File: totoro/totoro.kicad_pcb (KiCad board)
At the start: 2 copper layers, 82 parts, among them J1 USB_B_Micro, J2 SWR201-NRTN-S02-SA-WH, J3 SWR201-NRTN-S02-SA-WH, Q1 MMBT3904, Q2 MMBT3904, Q3 MMBT3904, Q4 2N7002, Q5 2N7002, Q6 MMBT3904, Q7 BC817, Q8 BC817, SW1 PTS810 SJM 250 SMTR LFS, SW2 KSC441J DCT 70SH LFS, U1 LMR62421XSD, U2 ESP32-WROOM-32, U3 CP2102N-A01-GQFN24, U4 TPS62152, U5 MCP6001R, U6 MCP6001R

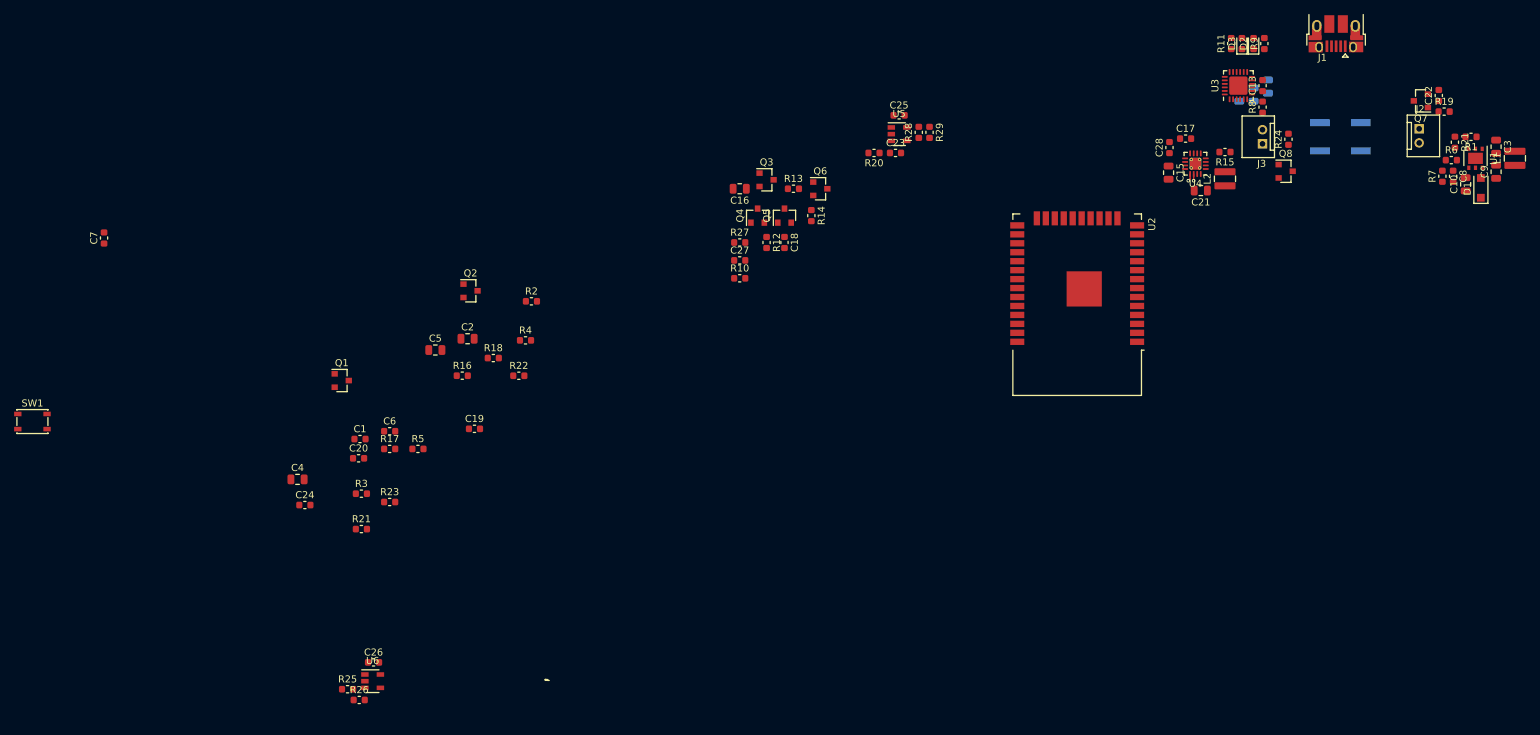
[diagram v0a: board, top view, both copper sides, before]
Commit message: All parts are in the circle
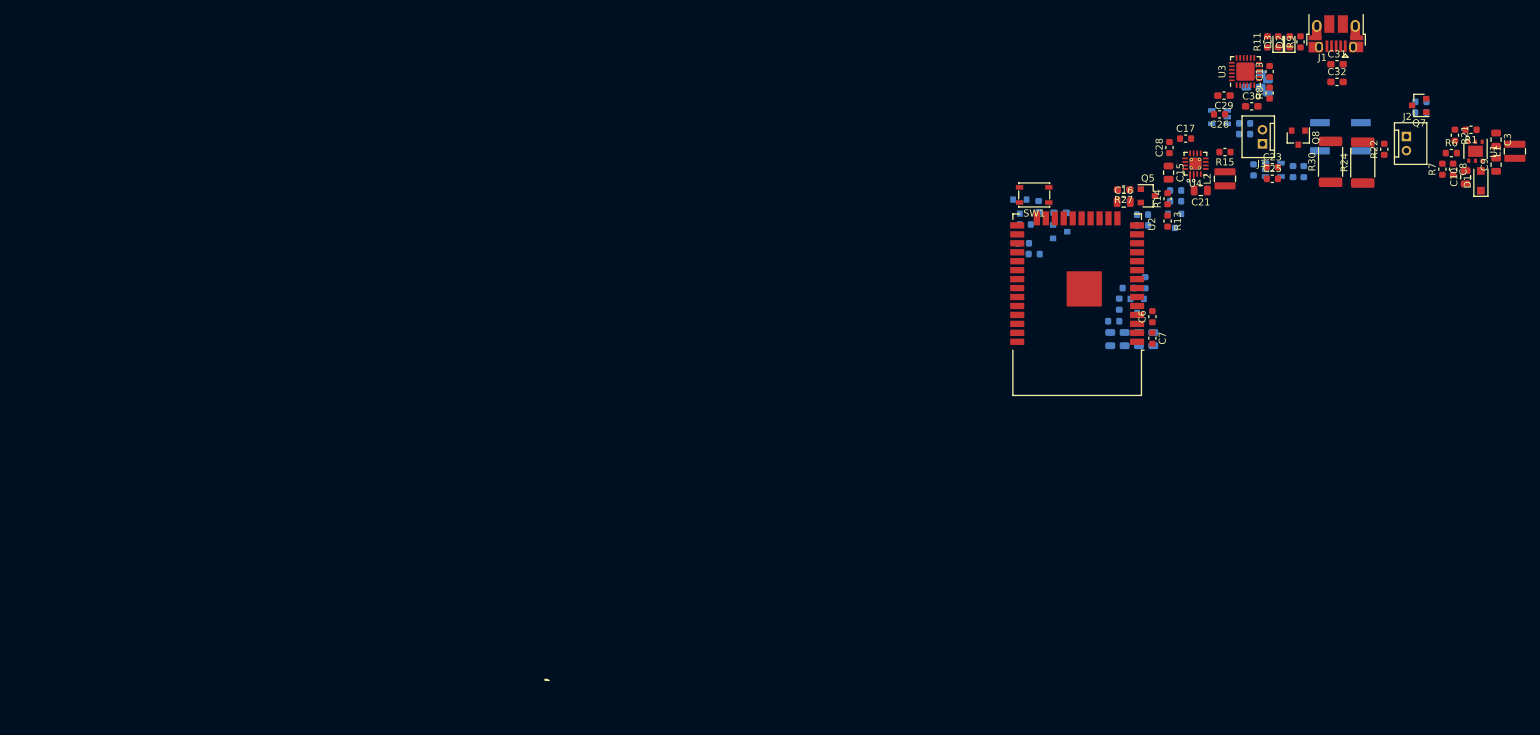
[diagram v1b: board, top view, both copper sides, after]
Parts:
- removed C27: 100nF, Capacitor_SMD:C_0603_1608Metric
- removed Q4: 2N7002, Package_TO_SOT_SMD:SOT-23
- removed the R21 at (290.7, 48.0)
- removed the R21 at (135.6, 102.9)
- added C29: 100nF, Capacitor_SMD:C_0603_1608Metric_Pad1.05x0.95mm_HandSolder, F.Cu at (257.9, 41.4)
- added C30: 100nF, Capacitor_SMD:C_0603_1608Metric_Pad1.05x0.95mm_HandSolder, F.Cu at (261.9, 42.9)
- added C31: 100nF, Capacitor_SMD:C_0603_1608Metric_Pad1.05x0.95mm_HandSolder, F.Cu at (274.0, 36.9)
- added C32: 100nF, Capacitor_SMD:C_0603_1608Metric_Pad1.05x0.95mm_HandSolder, F.Cu at (274.0, 39.5)
- added R21: 10k, Resistor_SMD:R_0603_1608Metric, F.Cu at (290.7, 47.0)
- added R30: 7.5, Resistor_SMD:R_2512_6332Metric, F.Cu at (273.0, 50.8)
- C1: footprint Capacitor_SMD:C_0603_1608Metric -> Capacitor_SMD:C_0805_2012Metric; moved to B.Cu
- C18, C19, C2, C20, C22, C24, C4, C5, Q1, Q2, Q3, Q6, R12, R16, R17, R18, R19, R2, R20, R23, R25, R26, R28, R29, R3, R4, R5, U5, U6: moved to B.Cu
- R10: value 10k -> 1k; footprint Resistor_SMD:R_0603_1608Metric -> Resistor_SMD:R_0603_1608Metric_Pad1.05x0.95mm_HandSolder; moved to B.Cu
- R24: value 3.71 -> 7.5; footprint Resistor_SMD:R_0603_1608Metric -> Resistor_SMD:R_2512_6332Metric
- R27: value 100 -> 100k; footprint Resistor_SMD:R_0603_1608Metric -> Resistor_SMD:R_0603_1608Metric_Pad1.05x0.95mm_HandSolder
- moved R25 150.4 mm to (260.8, 45.3), turned to 180 degrees
- moved C7 149.4 mm to (247.8, 75.8), turned to 270 degrees
- moved R26 149.1 mm to (260.8, 46.9)
- moved SW1 145.7 mm to (231.0, 55.5), turned to 180 degrees
- moved U6 144.3 mm to (257.3, 44.4), turned to 180 degrees
- moved C26 143.0 mm to (257.3, 44.1), turned to 180 degrees
- moved R22 126.9 mm to (280.7, 49.0), turned to 90 degrees
- moved C4 121.0 mm to (245.9, 75.9), turned to 270 degrees
- moved C24 120.8 mm to (244.3, 68.7), turned to 180 degrees
- moved Q1 113.3 mm to (245.6, 71.2), turned to 270 degrees
- moved R23 111.6 mm to (246.7, 67.9), turned to 270 degrees
- moved R17 111.4 mm to (246.4, 59.8), turned to 180 degrees
- moved R3 109.5 mm to (242.3, 73.4)
- moved C6 109.4 mm to (247.8, 72.8), turned to 90 degrees
- moved C1 107.4 mm to (241.8, 75.9), turned to 270 degrees
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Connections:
- C18 pad 1: Net-(C18-Pad1) -> PS_ENABLE
- Q3 pad 1: BATTERY+ -> OFF_SIGNAL
- Q3 pad 2: Net-(C16-Pad1) -> Net-(Q3-Pad2)
- Q3 pad 3: BATTERY+ -> OFF_SIGNAL
- Q5 pad 1: Net-(C18-Pad1) -> Net-(Q5-Pad1)
- Q5 pad 3: Net-(Q5-Pad3) -> PS_ENABLE
- Q6 pad 1: Net-(Q5-Pad3) -> Net-(Q6-Pad1)
- R10 pad 1: OFF_SIGNAL -> Net-(C16-Pad1)
- R10 pad 2: GND -> Net-(Q3-Pad2)
- R12 pad 1: Net-(C18-Pad1) -> Net-(Q5-Pad1)
- R13 pad 1: Net-(Q5-Pad3) -> Net-(Q6-Pad1)
- R14 pad 1: Net-(Q5-Pad3) -> Net-(Q6-Pad1)
- R27 pad 1: OFF_SIGNAL -> Net-(Q5-Pad1)
- R27 pad 2: Net-(Q4-Pad1) -> Net-(C16-Pad1)

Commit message: Drew board tentative outline
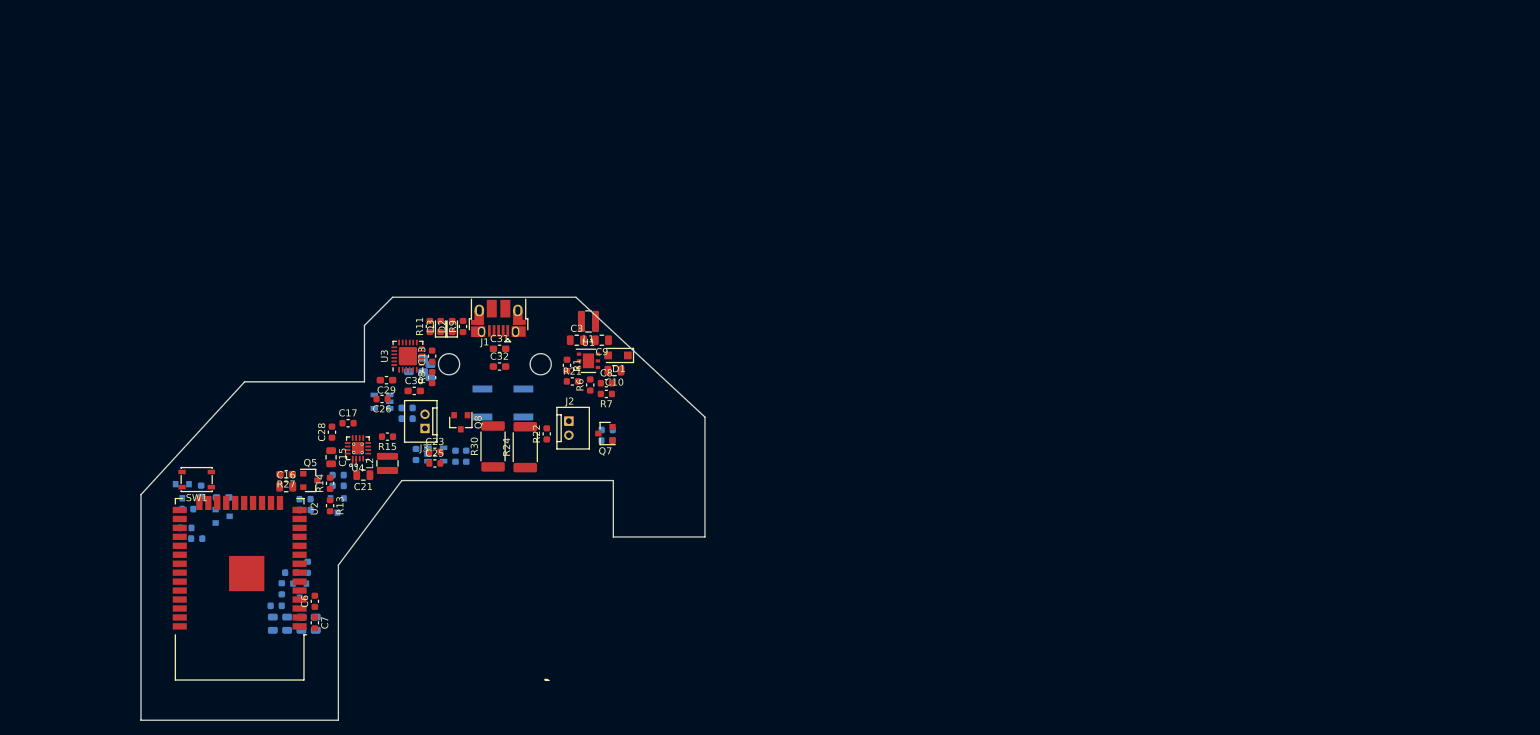
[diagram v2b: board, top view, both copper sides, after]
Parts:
- moved L1 133.6 mm to (167.8, 73.4), turned to 0 degrees
- moved C3 133.5 mm to (166.1, 76.1), turned to 0 degrees
- moved R1 132.5 mm to (164.7, 79.7), turned to 270 degrees
- moved R21 130.0 mm to (165.5, 81.9), turned to 0 degrees
- moved U1 129.3 mm to (167.8, 79.0), turned to 0 degrees
- moved C9 129.3 mm to (169.7, 76.1), turned to 180 degrees
- moved R6 126.5 mm to (168.0, 82.4), turned to 90 degrees
- moved C12 125.5 mm to (145.4, 80.5)
- moved C13 125.5 mm to (145.6, 78.4)
- moved C17 125.5 mm to (133.7, 87.9)
- moved C18 125.5 mm to (132.3, 95.2)
- moved C20 125.5 mm to (112.2, 104.2)
- moved C23 125.5 mm to (146.0, 91.9)
- moved C24 125.5 mm to (125.5, 109.1)
- moved C25 125.5 mm to (146.0, 93.6)
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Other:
- board outline added: 80 x 60 mm

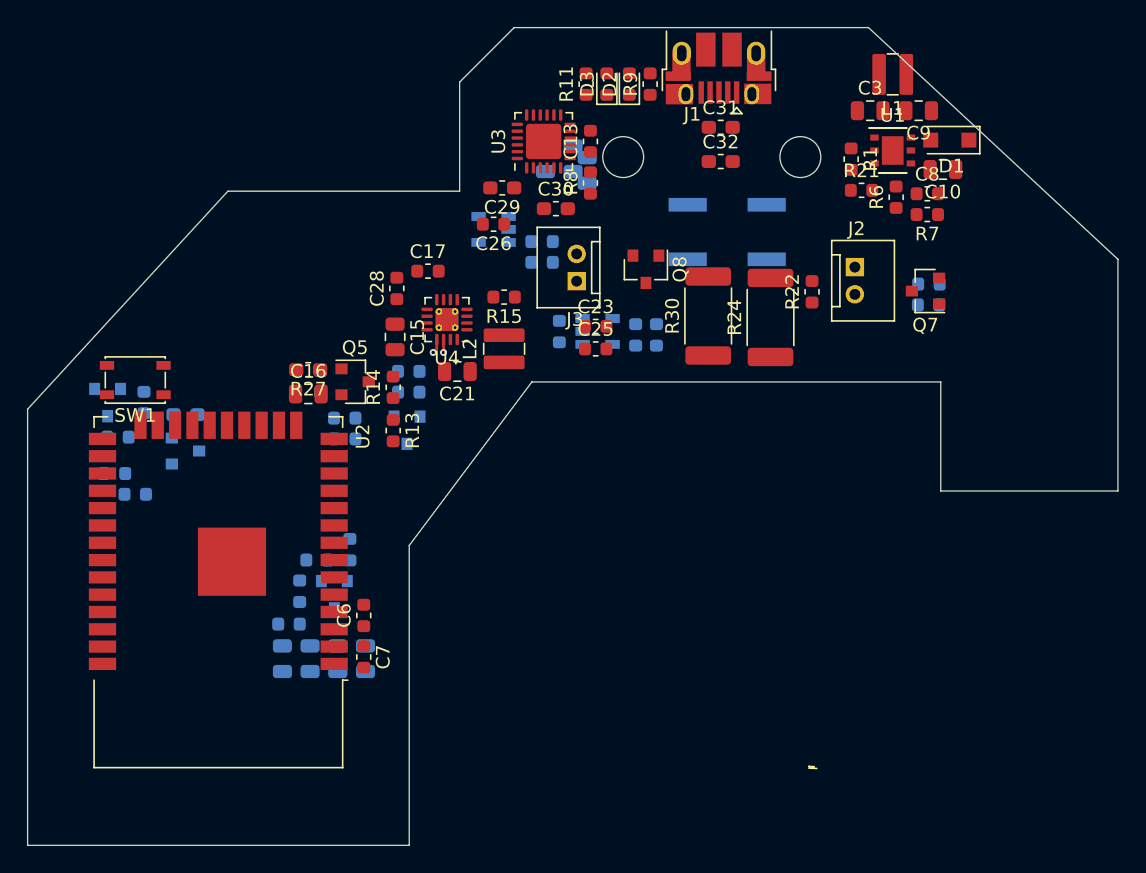
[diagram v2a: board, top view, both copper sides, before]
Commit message: Routed some traces. Shrunk board outline.
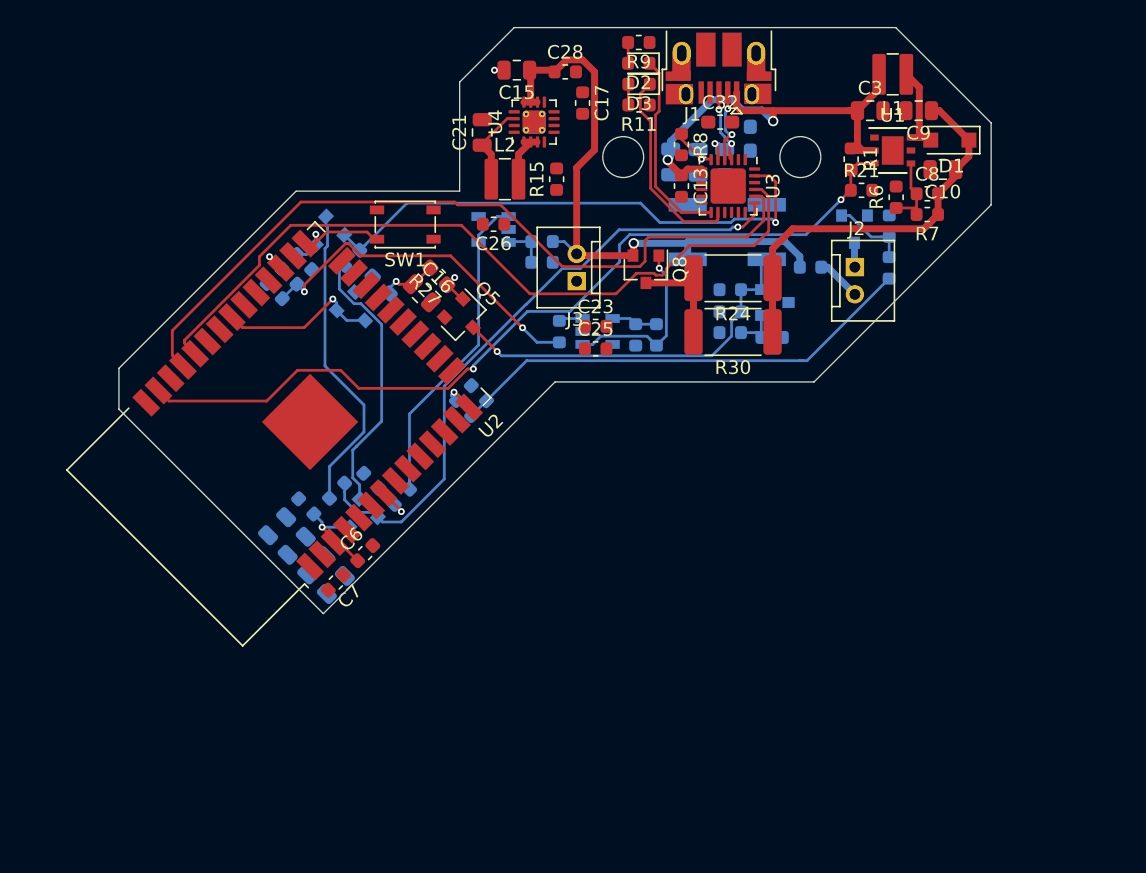
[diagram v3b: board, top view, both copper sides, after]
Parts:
- removed the C28 at (131.4, 89.1)
- removed C29, C30: 100nF, Capacitor_SMD:C_0603_1608Metric_Pad1.05x0.95mm_HandSolder
- added C20: 1uF, Capacitor_SMD:C_0603_1608Metric, B.Cu at (122.4, 89.3)
- C28: renamed from C20; value 1uF -> 100nF; moved to F.Cu
- C31, Q7, R13, R14, R22: moved to B.Cu
- moved C28 44.2 mm to (143.8, 73.2)
- moved R13 28.6 mm to (158.9, 92.7), turned to 0 degrees
- moved Q6 28.6 mm to (159.1, 90.2), turned to 0 degrees
- moved R14 25.1 mm to (155.9, 92.4), turned to 180 degrees
- moved R16 24.8 mm to (155.9, 89.2)
- moved C18 24.0 mm to (155.9, 90.9)
- moved SW1 22.9 mm to (132.0, 84.5)
- moved C15 21.5 mm to (140.2, 73.1), turned to 180 degrees
- moved Q2 20.2 mm to (126.2, 85.2), turned to 225 degrees
- moved R18 19.3 mm to (123.5, 88.3), turned to 135 degrees
- moved R5 18.8 mm to (124.6, 87.2), turned to 135 degrees
- moved R2 18.6 mm to (128.1, 86.9), turned to 45 degrees
- moved C21 17.6 mm to (137.7, 77.7), turned to 90 degrees
- moved R10 17.2 mm to (130.2, 88.9), turned to 135 degrees
- moved C17 16.8 mm to (145.0, 75.5), turned to 270 degrees
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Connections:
- C28 pad 1: Net-(C20-Pad1) -> BATTERY+
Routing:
- net CHARGE_ENABLE: track 0.00 -> 62.9 mm, vias 0 -> 2
- net PROG_RX: track 0.00 -> 56.8 mm
- net PROG_TX: track 0.00 -> 56.0 mm
- net PROG_RTS: track 0.00 -> 46.2 mm, vias 0 -> 1
- net BATTERY+: track 0.00 -> 44.8 mm, vias 0 -> 1
- net PROG_DTR: track 0.00 -> 39.0 mm, vias 0 -> 1
- net Net-(C19-Pad1): track 0.00 -> 35.0 mm
- net USB_VIN: track 0.00 -> 33.5 mm, vias 0 -> 2
- net +6V: track 0.00 -> 30.6 mm
- net PS_ENABLE: track 1.06 -> 28.0 mm
- net Net-(C20-Pad1): track 0.00 -> 25.8 mm, vias 0 -> 2
- net Net-(R23-Pad1): track 0.00 -> 23.5 mm
- net Net-(Q2-Pad1): track 0.00 -> 23.0 mm
- net Net-(Q1-Pad1): track 0.00 -> 20.0 mm
- net Net-(D3-Pad1): track 0.00 -> 14.8 mm
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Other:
- board size 80 x 60 mm -> 64 x 43 mm
- copper layers 2 -> 4
- net class Power added: clearance 0.1524, trace_width 0.508, via_dia 0.762, via_drill 0.508
